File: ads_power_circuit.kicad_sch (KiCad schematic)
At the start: 3 parts, among them K1 KSW80

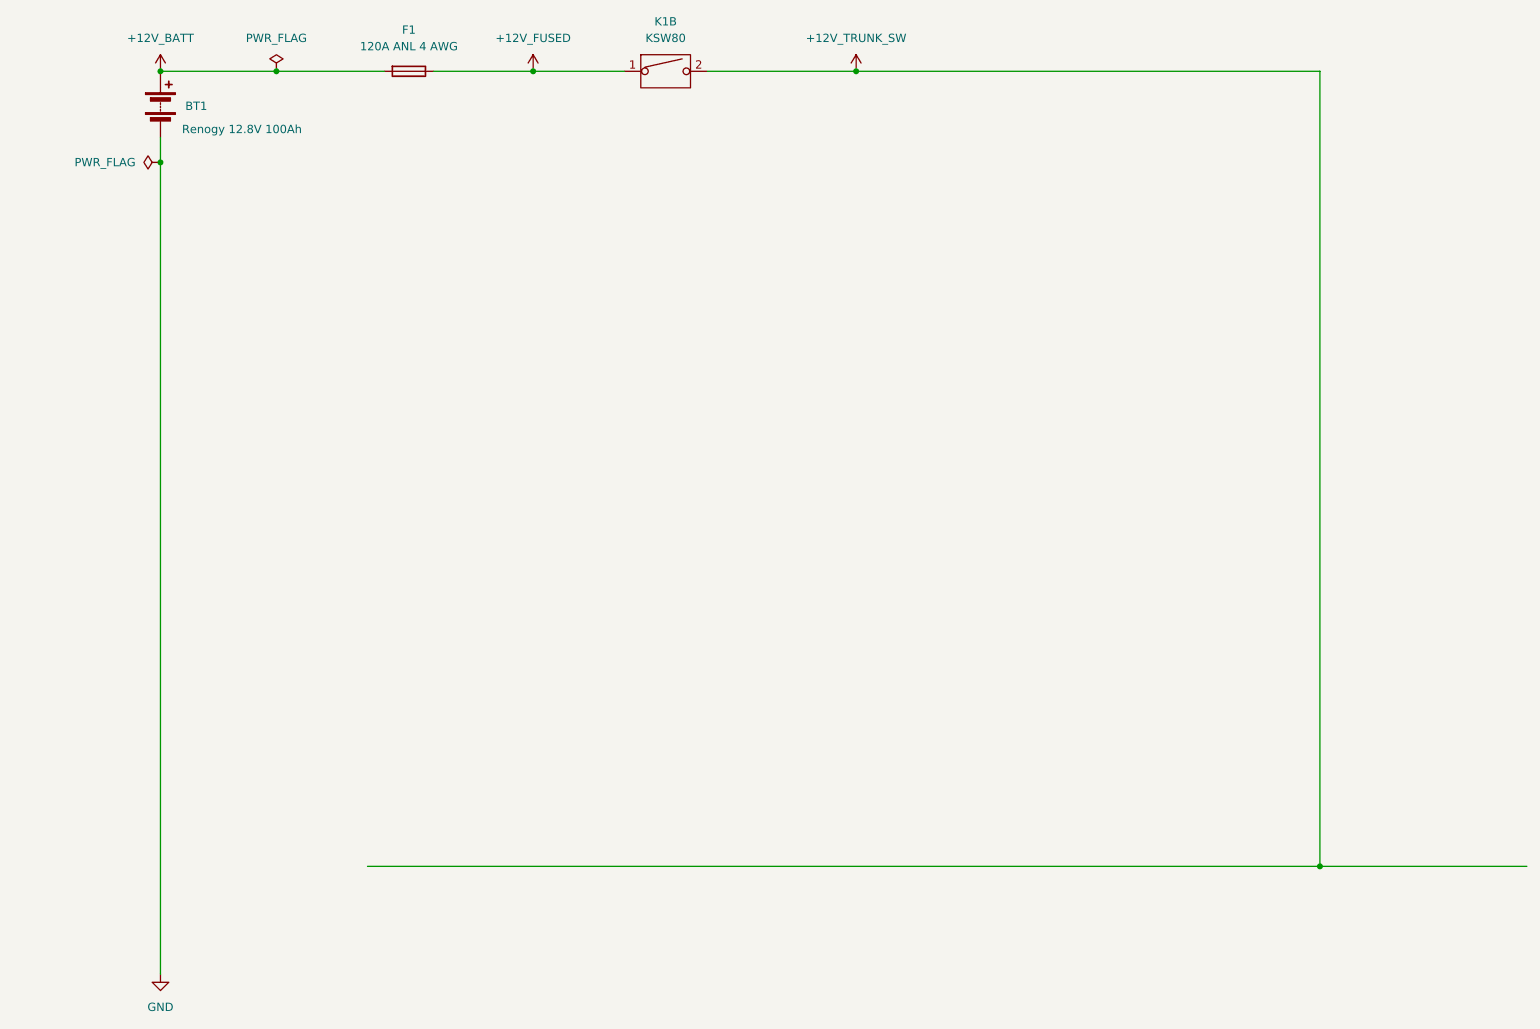
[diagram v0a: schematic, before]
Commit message: Finalised first draft of ADS power spine with all fuses and converters. Some fuses still need validation!
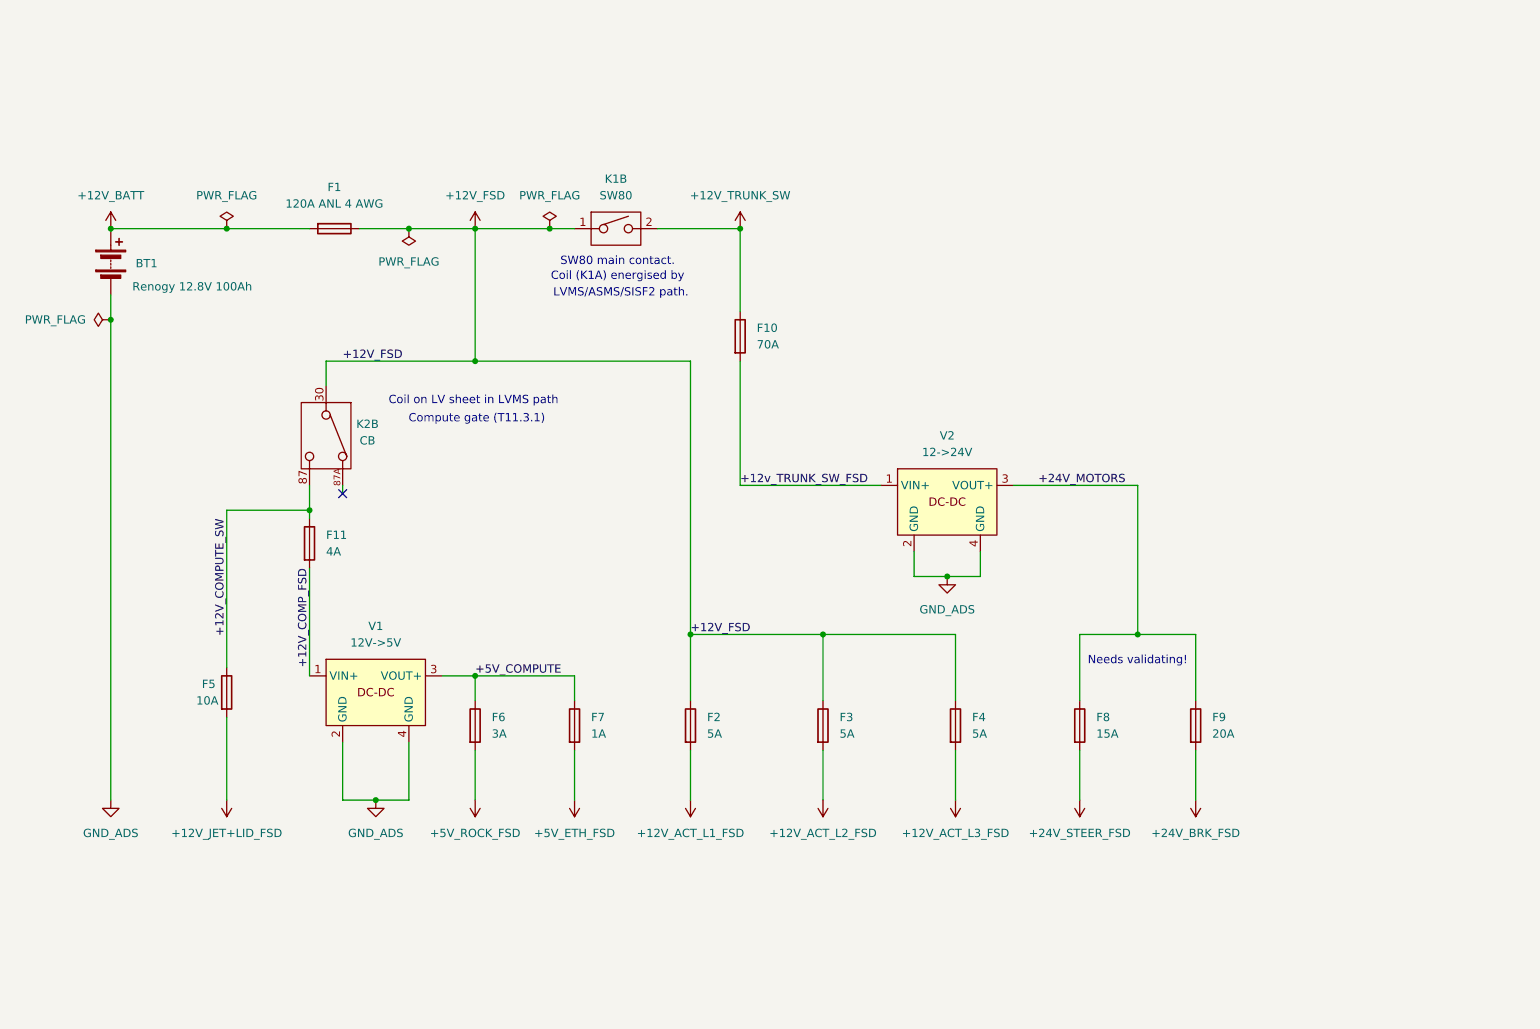
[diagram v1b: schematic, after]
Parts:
- added F10: 70A, symbol Device:Fuse
- added F11: 4A, symbol Device:Fuse
- added F2, F3, F4: 5A, symbol Device:Fuse
- added F5: 10A, symbol Device:Fuse
- added F6: 3A, symbol Device:Fuse
- added F7: 1A, symbol Device:Fuse
- added F8: 15A, symbol Device:Fuse
- added F9: 20A, symbol Device:Fuse
- added K2: CB, symbol FSUK_ADS:RELAY_COMP_SPDT
- added V1: 12V->5V, symbol FSUK_ADS:Voltage_Converter
- added V2: 12->24V, symbol FSUK_ADS:Voltage_Converter
- K1: value KSW80 -> SW80
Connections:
- net +12V_TRUNK_SW: now also F10.1
- net +12V_FUSED renamed +12V_FSD
- net +12V_FSD: now also F2.1, F3.1, F4.1, K2.30 (POLE)
- net GND renamed GND_ADS
- net GND_ADS: now also V1.2 (GND), V1.4 (GND), V2.2 (GND), V2.4 (GND)
- new net +12V_ACT_L1_FSD: F2.2
- new net +12V_ACT_L2_FSD: F3.2
- new net +12V_ACT_L3_FSD: F4.2
- new net +12V_COMPUTE_SW: F11.1, F5.1, K2.87 (NO)
- new net +12V_COMP_FSD: F11.2, V1.1 (VIN+)
- new net +12V_JET+LID_FSD: F5.2
- new net +12v_TRUNK_SW_FSD: F10.2, V2.1 (VIN+)
- new net +24V_BRK_FSD: F9.2
- new net +24V_MOTORS: F8.1, F9.1, V2.3 (VOUT+)
- new net +24V_STEER_FSD: F8.2
- new net +5V_COMPUTE: F6.1, F7.1, V1.3 (VOUT+)
- new net +5V_ETH_FSD: F7.2
- new net +5V_ROCK_FSD: F6.2
- no-connect marks 0 -> 1
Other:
- note added: "Coil (K1A) energised by"
- note added: "Coil on LV sheet in LVMS path"
- note added: "Compute gate (T11.3.1)"
- note added: "LVMS/ASMS/SISF2 path."
- note added: "Needs validating!"
- note added: "SW80 main contact."
- moved on the sheet: BT1, F1

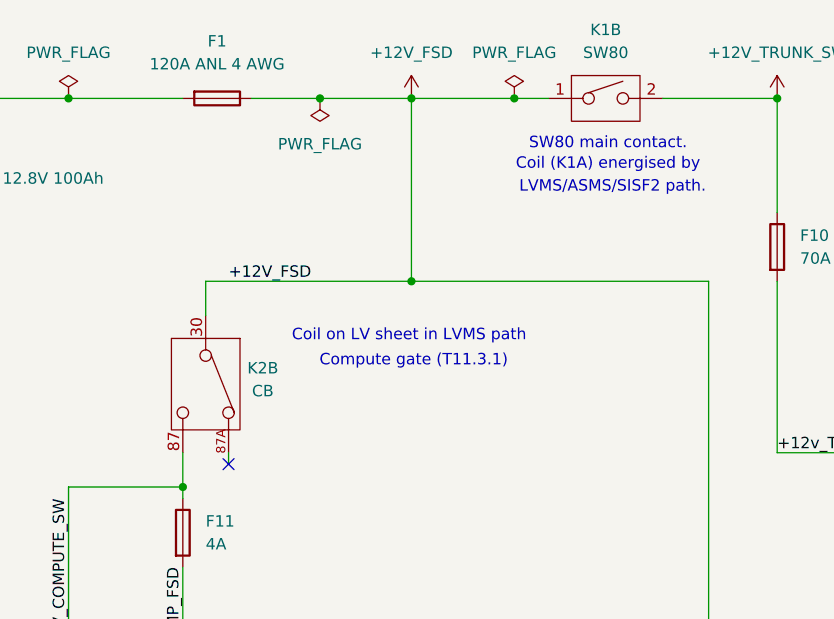
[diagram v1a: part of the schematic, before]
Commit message: Designed SISF2 and edited relay symbols to have pin names on outside
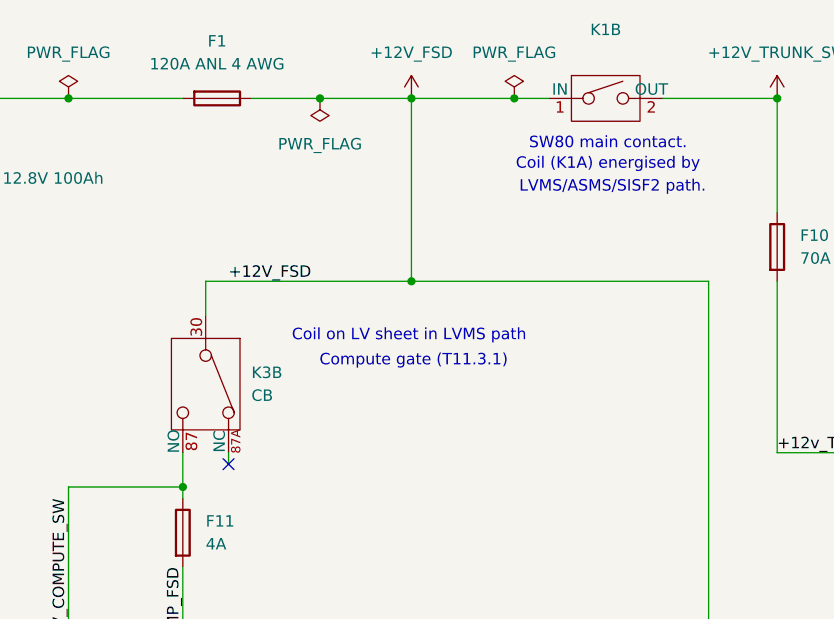
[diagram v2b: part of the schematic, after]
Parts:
- removed K2: CB, symbol FSUK_ADS:RELAY_COMP_SPDT
- added K3: CB, symbol FSUK_ADS:RELAY_COMP_SPDT
- K1: value SW80 -> ~
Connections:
- net +12V_COMPUTE_SW: now also K3.87 (NO)
- net +12V_FSD: now also K3.30

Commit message: Had not saved changes, this commit is for the last one :)
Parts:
- K1: value ~ -> SW80
- K3: value CB -> COMPUTE
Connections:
- net +12V_TRUNK_SW renamed +12v_TRUNK_SW
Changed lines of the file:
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@@
-	)
-	(junction
-		(at 139.7 49.53)
-		(diameter 0)
-		(color 0 0 0 0)
 	)
 	(junction
@@
 		)
 	)
+	(label "+12v_TRUNK_SW"
+		(at 132.08 49.53 0)
+		(effects
+			(font
+				(size 1.27 1.27)
+			)
+			(justify left bottom)
+		)
+	)
 	(label "+24V_MOTORS"
 		(at 185.42 88.9 0)
@@
 			)
 		)
-		(property "Value" "~"
+		(property "Value" "SW80"
 			(at 120.65 44.45 0)
 			(effects
@@
 				(path "/d6aff74e-3318-4fd0-8dc7-ec5368c0dfa8/b502e227-70b4-4105-b13f-6ec8a9fa398b"
 					(reference "V2")
-					(unit 1)
-				)
-			)
-		)
-	)
-	(symbol
-		(lib_id "FSUK_ADS:+12V_TRUNK_SW")
-		(at 139.7 49.53 0)
-		(unit 1)
-		(exclude_from_sim no)
-		(in_bom yes)
-		(on_board yes)
-		(dnp no)
-		(fields_autoplaced yes)
-		(property "Reference" "#PWR04"
-			(at 139.7 53.34 0)
-			(effects
-				(font
-					(size 1.27 1.27)
-				)
-				(hide yes)
-			)
-		)
-		(property "Value" "+12V_TRUNK_SW"
-			(at 139.7 44.45 0)
-			(effects
-				(font
-					(size 1.27 1.27)
-				)
-			)
-		)
-		(property "Footprint" ""
-			(at 139.7 49.53 0)
-			(effects
-				(font
-					(size 1.27 1.27)
-				)
-				(hide yes)
-			)
-		)
-		(property "Datasheet" ""
-			(at 139.7 49.53 0)
-			(effects
-				(font
-					(size 1.27 1.27)
-				)
-				(hide yes)
-			)
-		)
-		(property "Description" "Power symbol creates a global label with name \"+12V\""
-			(at 139.7 49.53 0)
-			(effects
-				(font
-					(size 1.27 1.27)
-				)
-				(hide yes)
-			)
-		)
-		(pin "1"
-		)
-		(instances
-			(project "fsuk-ads-electrical"
-				(path "/d6aff74e-3318-4fd0-8dc7-ec5368c0dfa8/b502e227-70b4-4105-b13f-6ec8a9fa398b"
-					(reference "#PWR04")
 					(unit 1)
 				)
@@
 			)
 		)
-		(property "Value" "CB"
+		(property "Value" "COMPUTE"
 			(at 81.28 82.5499 90)
 			(effects
